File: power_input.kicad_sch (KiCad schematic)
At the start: 17 parts, among them J4 12V -, J5 12V +, U6 TPS565242

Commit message: latest
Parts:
- removed D6: SS54, Diode_SMD:D_SMA, symbol Device:D_Schottky
- added C41, C42: 100nF, Capacitor_SMD:C_0402_1005Metric, symbol Device:C_Small
- added D15: LED, LED_SMD:LED_0805_2012Metric, symbol Device:LED
- added D6: MMSZ18T1G, Diode_SMD:D_SOD-123, symbol Device:D_Zener
- added Q1: AONR21321, Transistor_Power_Module:TRANS_AONR21321, symbol AONR21321:AONR21321
- added R7: 470, Resistor_SMD:R_0603_1608Metric, symbol Device:R_Small_US
- added R9: 100K, Resistor_SMD:R_0402_1005Metric, symbol Device:R_Small_US
- C25, C26: value 10µF -> 10uF
- C27: value 0.1µF -> 100nF
- C28, C29, C30: value 22µF -> 22uF
- FB1: value 600R/3A -> HCB3216KF-601T30; footprint Capacitor_SMD:C_0805_2012Metric -> Capacitor_SMD:C_1206_3216Metric
- R11: value 20KΩ -> 20K
- R12, R14: value 30KΩ -> 30K; footprint Resistor_SMD:R_0402_1005Metric -> Resistor_SMD:R_0603_1608Metric
- R13: value 220KΩ -> 220K; footprint Resistor_SMD:R_0402_1005Metric -> Resistor_SMD:R_0603_1608Metric
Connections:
- net +5V: now also R7.2
- net WG_+12V: now also C42.1, D6.1 (K), Q1.1, Q1.2, Q1.3
- net at J5.1 (Pin_1): now also C41.1, Q1.5, Q1.6, Q1.7, Q1.8, Q1.9, Q1.9_1, Q1.9_2
- new net: D6.2 (A), Q1.4, R9.2
- new net: D15.2 (A), R7.1
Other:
- moved on the sheet: J4, J5

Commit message: starting pd chip
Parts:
- added C45, C46: 1uF, symbol Device:C_Small
- added U11: XC6206PxxxMR, Package_TO_SOT_SMD:SOT-23-3, symbol Regulator_Linear:XC6206PxxxMR
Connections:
- net +5V: now also C45.1, U11.3 (VI)
- new net +3V3: C46.1, U11.2 (VO)

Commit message: added footprints, minor deletions
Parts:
- C45, C46: footprint (none) -> Capacitor_SMD:C_0402_1005Metric
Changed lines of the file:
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@@
 			)
 		)
-		(property "Footprint" ""
+		(property "Footprint" "Capacitor_SMD:C_0402_1005Metric"
 			(at 168.91 66.04 0)
 			(effects
@@
 			)
 		)
-		(property "Footprint" ""
+		(property "Footprint" "Capacitor_SMD:C_0402_1005Metric"
 			(at 146.05 66.04 0)
 			(effects

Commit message: add usb-c-pd routing
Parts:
- D15: footprint LED_SMD:LED_0805_2012Metric -> LED_SMD:LED_0603_1608Metric
- R7: footprint Resistor_SMD:R_0603_1608Metric -> Resistor_SMD:R_0402_1005Metric
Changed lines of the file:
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@@
 			)
 		)
-		(property "Footprint" "Resistor_SMD:R_0603_1608Metric"
+		(property "Footprint" "Resistor_SMD:R_0402_1005Metric"
 			(at 100.33 74.93 0)
 			(effects
@@
 			)
 		)
-		(property "Footprint" "LED_SMD:LED_0805_2012Metric"
+		(property "Footprint" "LED_SMD:LED_0603_1608Metric"
 			(at 93.98 74.93 0)
 			(effects

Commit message: new buck
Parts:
- removed D5: 1N4148WS, Diode_SMD:D_SOD-323, symbol Diode:1N4148WS
- removed R14: 30K, Resistor_SMD:R_0603_1608Metric, symbol Device:R_Small_US
- removed U6: TPS565242, Package_TO_SOT_SMD:SOT6_DRL_TEX-L, symbol Regulator_Switching:TPS565242
- added C59, C60: 22 uF, symbol Device:C_Small
- added U6: LMR33640ADDA, Package_SO:Texas_HSOP-8-1EP_3.9x4.9mm_P1.27mm_ThermalVias, symbol Regulator_Switching:LMR33640ADDA
- C25: value 10uF -> 220 nF
- C26: value 10uF -> 10 uF
- C27: value 100nF -> 1 uF
- C28: value 22uF -> 100 nF; footprint Capacitor_SMD:C_0603_1608Metric -> (none)
- C29, C30: value 22uF -> 22 uF; footprint Capacitor_SMD:C_0603_1608Metric -> (none)
- L1: value SPM6530T-2R2M -> L; footprint Inductor_SMD:IND_SPM6530T-2R2M -> (none)
- R11: value 20K -> 100k
- R12: value 30K -> 100k; footprint Resistor_SMD:R_0603_1608Metric -> (none)
- R13: value 220K -> 24.9k; footprint Resistor_SMD:R_0603_1608Metric -> (none)
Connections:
- net WG_+12V: now also U6.2 (VIN), U6.3 (EN); no longer C27.1, R11.1
- net at C29.1, C30.1, FB1.2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: now also R12.1, C59.1, C60.1; no longer C28.1, R13.2
- net at L1.1: now also C28.2, U6.8 (SW)
- net at R11.2: now also C27.1, U6.6 (VCC); no longer R12.1
- net at R13.1: now also R12.2, U6.5 (FB)
- net at C26.2: now also C25.2
- new net: U6.1 (GND), U6.9 (GND)
- new net: R11.1, U6.4 (PG)
- new net: C28.1, U6.7 (BOOT)
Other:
- moved on the sheet: FB1

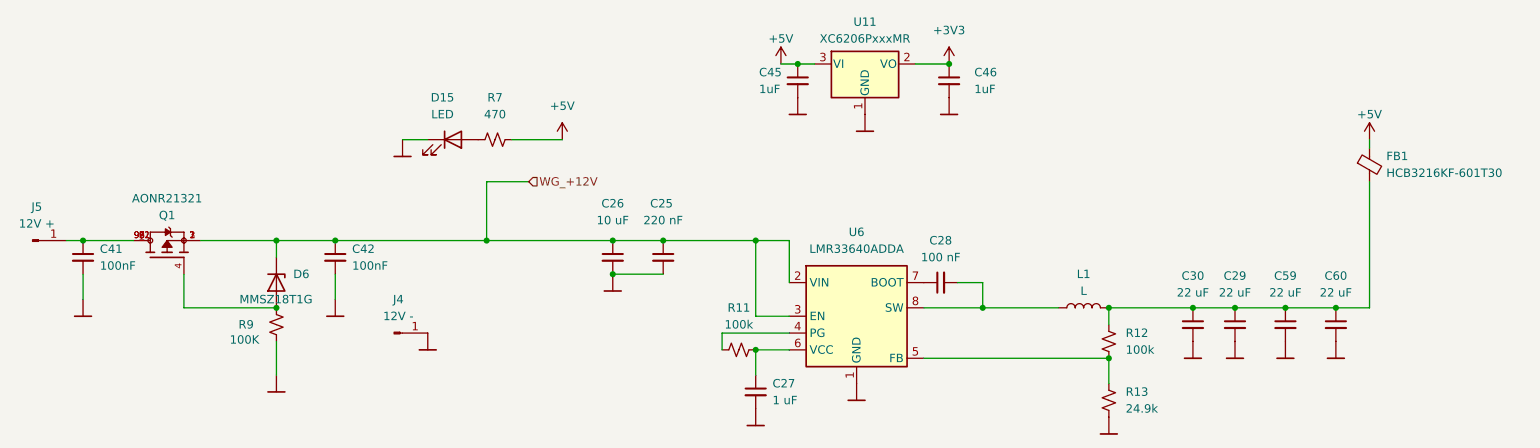
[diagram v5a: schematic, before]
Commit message: new power supply
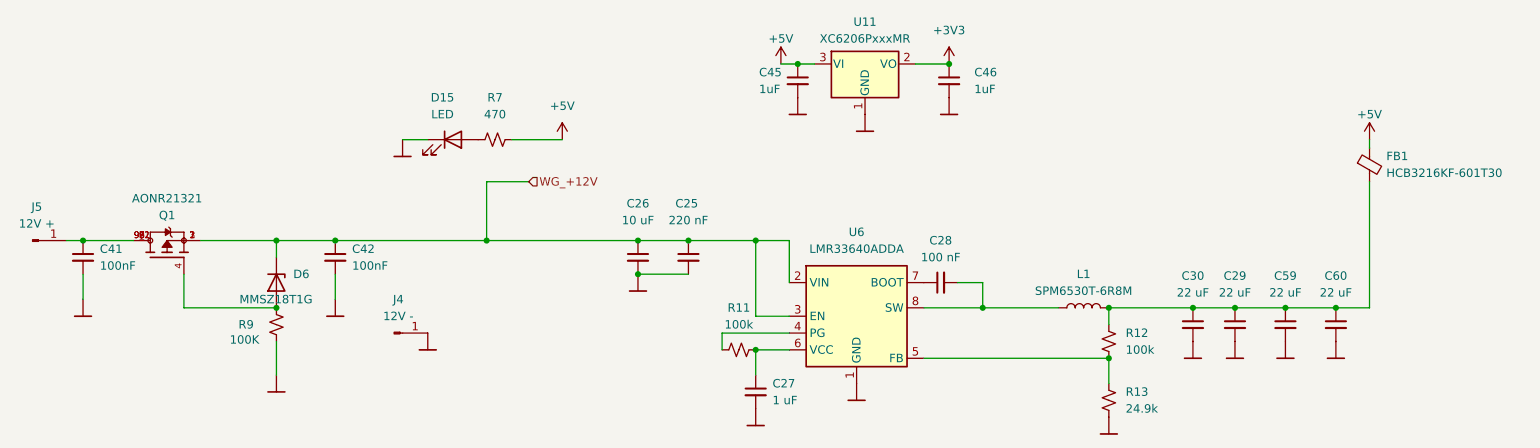
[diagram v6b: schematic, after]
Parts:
- C28, C29, C30, C59, C60, R12: footprint (none) -> Capacitor_SMD:C_0402_1005Metric
- L1: value L -> SPM6530T-6R8M; footprint (none) -> Inductor_SMD:IND_SPM6530T-2R2M
- R13: footprint (none) -> Resistor_SMD:R_0402_1005Metric
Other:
- moved on the sheet: C25, C26
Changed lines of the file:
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@@
 	)
 	(junction
+		(at 121.92 95.25)
+		(diameter 0)
+		(color 0 0 0 0)
+	)
+	(junction
+		(at 129.54 90.17)
+		(diameter 0)
+		(color 0 0 0 0)
+	)
+	(junction
 		(at 76.2 90.17)
 		(diameter 0)
@@
 	)
 	(junction
-		(at 118.11 90.17)
+		(at 99.06 90.17)
 		(diameter 0)
 		(color 0 0 0 0)
 	)
 	(junction
-		(at 99.06 90.17)
+		(at 121.92 90.17)
 		(diameter 0)
 		(color 0 0 0 0)
@@
 	)
 	(junction
-		(at 125.73 90.17)
-		(diameter 0)
-		(color 0 0 0 0)
-	)
-	(junction
 		(at 38.1 90.17)
 		(diameter 0)
@@
 	)
 	(junction
-		(at 118.11 95.25)
-		(diameter 0)
-		(color 0 0 0 0)
-	)
-	(junction
 		(at 205.74 100.33)
 		(diameter 0)
@@
 	(wire
 		(pts
-			(xy 125.73 90.17) (xy 139.7 90.17)
-		)
-		(stroke
-			(width 0)
-			(type default)
-		)
-	)
-	(wire
-		(pts
 			(xy 67.31 90.17) (xy 67.31 92.71)
 		)
@@
 	(wire
 		(pts
-			(xy 99.06 90.17) (xy 118.11 90.17)
+			(xy 99.06 90.17) (xy 121.92 90.17)
 		)
 		(stroke
@@
 	(wire
 		(pts
-			(xy 118.11 95.25) (xy 125.73 95.25)
-		)
-		(stroke
-			(width 0)
-			(type default)
-		)
-	)
-	(wire
-		(pts
 			(xy 134.62 104.14) (xy 134.62 106.68)
 		)
@@
 	(wire
 		(pts
-			(xy 118.11 90.17) (xy 125.73 90.17)
+			(xy 121.92 90.17) (xy 129.54 90.17)
 		)
 		(stroke
@@
 	(wire
 		(pts
+			(xy 129.54 90.17) (xy 139.7 90.17)
+		)
+		(stroke
+			(width 0)
+			(type default)
+		)
+	)
+	(wire
+		(pts
+			(xy 121.92 95.25) (xy 129.54 95.25)
+		)
+		(stroke
+			(width 0)
+			(type default)
+		)
+	)
+	(wire
+		(pts
 			(xy 67.31 90.17) (xy 76.2 90.17)
 		)
@@
 		(dnp no)
 		(fields_autoplaced yes)
-		(property "Reference" "01"
+		(property "Reference" "#0120"
 			(at 193.04 119.38 0)
 			(effects
@@
 			(project ""
 				(path "/6ff0ef20-ee81-4b16-8d31-a8f0cc267b22/8f744145-cbac-43cd-8d9b-32558df82040"
-					(reference "01")
+					(reference "#0120")
 					(unit 1)
 				)
@@
 		(dnp no)
 		(fields_autoplaced yes)
-		(property "Reference" "01"
+		(property "Reference" "#0112"
 			(at 154.94 114.3 0)
 			(effects
@@
 			(project ""
 				(path "/6ff0ef20-ee81-4b16-8d31-a8f0cc267b22/8f744145-cbac-43cd-8d9b-32558df82040"
-					(reference "01")
+					(reference "#0112")
 					(unit 1)
 				)
@@
 			)
 		)
-		(property "Footprint" ""
+		(property "Footprint" "Resistor_SMD:R_0402_1005Metric"
 			(at 193.04 114.3 0)
 			(effects
@@
 			)
 		)
-		(property "Footprint" ""
+		(property "Footprint" "Capacitor_SMD:C_0402_1005Metric"
 			(at 193.04 105.41 0)
 			(effects
@@
 		(dnp no)
 		(fields_autoplaced yes)
-		(property "Reference" "0101"
+		(property "Reference" "#0122"
 			(at 212.09 107.95 0)
 			(effects
@@
 			(project "wind board"
 				(path "/6ff0ef20-ee81-4b16-8d31-a8f0cc267b22/8f744145-cbac-43cd-8d9b-32558df82040"
-					(reference "0101")
+					(reference "#0122")
 					(unit 1)
 				)
@@
 	(symbol
 		(lib_id "Device:C_Small")
-		(at 125.73 92.71 0)
+		(at 129.54 92.71 0)
 		(unit 1)
 		(exclude_from_sim no)
@@
 		(dnp no)
 		(property "Reference" "C25"
-			(at 125.476 84.582 0)
+			(at 129.286 84.582 0)
 			(effects
 				(font
@@
 		)
 		(property "Value" "220 nF"
-			(at 125.73 87.122 0)
+			(at 129.54 87.122 0)
 			(effects
 				(font
@@
 		)
 		(property "Footprint" "Capacitor_SMD:C_0402_1005Metric"
-			(at 125.73 92.71 0)
+			(at 129.54 92.71 0)
 			(effects
 				(font
@@
 		)
 		(property "Datasheet" "~"
-			(at 125.73 92.71 0)
+			(at 129.54 92.71 0)
 			(effects
 				(font
@@
 		)
 		(property "Description" "Unpolarized capacitor, small symbol"
-			(at 125.73 92.71 0)
+			(at 129.54 92.71 0)
 			(effects
 				(font
@@
 			)
 		)
-		(property "Footprint" ""
+		(property "Footprint" "Capacitor_SMD:C_0402_1005Metric"
 			(at 227.33 102.87 0)
 			(effects
@@
 		(dnp no)
 		(fields_autoplaced yes)
-		(property "Reference" "0101"
+		(property "Reference" "#0123"
 			(at 205.74 107.95 0)
 			(effects
@@
 			(project "wind board"
 				(path "/6ff0ef20-ee81-4b16-8d31-a8f0cc267b22/8f744145-cbac-43cd-8d9b-32558df82040"
-					(reference "0101")
+					(reference "#0123")
 					(unit 1)
 				)
@@
 		(dnp no)
 		(fields_autoplaced yes)
-		(property "Reference" "01"
+		(property "Reference" "#0113"
 			(at 139.7 118.11 0)
 			(effects
@@
 			(project ""
 				(path "/6ff0ef20-ee81-4b16-8d31-a8f0cc267b22/8f744145-cbac-43cd-8d9b-32558df82040"
-					(reference "01")
+					(reference "#0113")
 					(unit 1)
 				)
@@
 			)
 		)
-		(property "Footprint" ""
+		(property "Footprint" "Capacitor_SMD:C_0402_1005Metric"
 			(at 205.74 102.87 0)
 			(effects
@@
 		(dnp no)
 		(fields_autoplaced yes)
-		(property "Reference" "0101"
+		(property "Reference" "#0126"
 			(at 219.71 107.95 0)
 			(effects
@@
 			(project "wind board"
 				(path "/6ff0ef20-ee81-4b16-8d31-a8f0cc267b22/8f744145-cbac-43cd-8d9b-32558df82040"
-					(reference "0101")
+					(reference "#0126")
 					(unit 1)
 				)
@@
 		(dnp no)
 		(fields_autoplaced yes)
-		(property "Reference" "01"
+		(property "Reference" "#0121"
 			(at 227.33 107.95 0)
 			(effects
@@
 			(project ""
 				(path "/6ff0ef20-ee81-4b16-8d31-a8f0cc267b22/8f744145-cbac-43cd-8d9b-32558df82040"
-					(reference "01")
+					(reference "#0121")
 					(unit 1)
 				)
@@
 			)
 		)
-		(property "Footprint" ""
+		(property "Footprint" "Capacitor_SMD:C_0402_1005Metric"
 			(at 219.71 102.87 0)
 			(effects
@@
 	(symbol
 		(lib_id "Device:C_Small")
-		(at 118.11 92.71 0)
+		(at 121.92 92.71 0)
 		(unit 1)
 		(exclude_from_sim no)
@@
 		(dnp no)
 		(property "Reference" "C26"
-			(at 118.11 84.582 0)
+			(at 121.92 84.582 0)
 			(effects
 				(font
@@
 		)
 		(property "Value" "10 uF"
-			(at 118.11 87.122 0)
+			(at 121.92 87.122 0)
 			(effects
 				(font
@@
 		)
 		(property "Footprint" "Capacitor_SMD:C_0402_1005Metric"
-			(at 118.11 92.71 0)
+			(at 121.92 92.71 0)
 			(effects
 				(font
@@
 		)
 		(property "Datasheet" "~"
-			(at 118.11 92.71 0)
+			(at 121.92 92.71 0)
 			(effects
 				(font
@@
 		)
 		(property "Description" "Unpolarized capacitor, small symbol"
-			(at 118.11 92.71 0)
+			(at 121.92 92.71 0)
 			(effects
 				(font
@@
 	(symbol
 		(lib_id "power:GND")
-		(at 118.11 97.79 0)
+		(at 121.92 97.79 0)
 		(unit 1)
 		(exclude_from_sim no)
@@
 		(dnp no)
 		(fields_autoplaced yes)
-		(property "Reference" "01"
-			(at 118.11 97.79 0)
+		(property "Reference" "#0124"
+			(at 121.92 97.79 0)
 			(effects
 				(font
@@
 		)
 		(property "Value" "~"
-			(at 118.11 100.33 0)
+			(at 121.92 100.33 0)
 			(effects
 				(font
@@
 		)
 		(property "Footprint" ""
-			(at 118.11 97.79 0)
+			(at 121.92 97.79 0)
 			(effects
 				(font
@@
 		)
 		(property "Datasheet" ""
-			(at 118.11 97.79 0)
+			(at 121.92 97.79 0)
 			(effects
 				(font
@@
 		)
 		(property "Description" "GND"
-			(at 118.11 97.79 0)
+			(at 121.92 97.79 0)
 			(effects
 				(font
@@
 			(project ""
 				(path "/6ff0ef20-ee81-4b16-8d31-a8f0cc267b22/8f744145-cbac-43cd-8d9b-32558df82040"
-					(reference "01")
+					(reference "#0124")
 					(unit 1)
 				)
@@
 			)
 		)
-		(property "Value" "L"
+		(property "Value" "SPM6530T-6R8M"
 			(at 189.23 97.79 90)
 			(effects
@@
 			)
 		)
-		(property "Footprint" ""
+		(property "Footprint" "Inductor_SMD:IND_SPM6530T-2R2M"
 			(at 189.23 100.33 0)
 			(effects
@@
 			)
 		)
-		(property "Footprint" ""
+		(property "Footprint" "Capacitor_SMD:C_0402_1005Metric"
 			(at 212.09 102.87 0)
 			(effects
@@
 			)
 		)
-		(property "Footprint" ""
+		(property "Footprint" "Capacitor_SMD:C_0402_1005Metric"
 			(at 167.64 96.52 0)
 			(effects

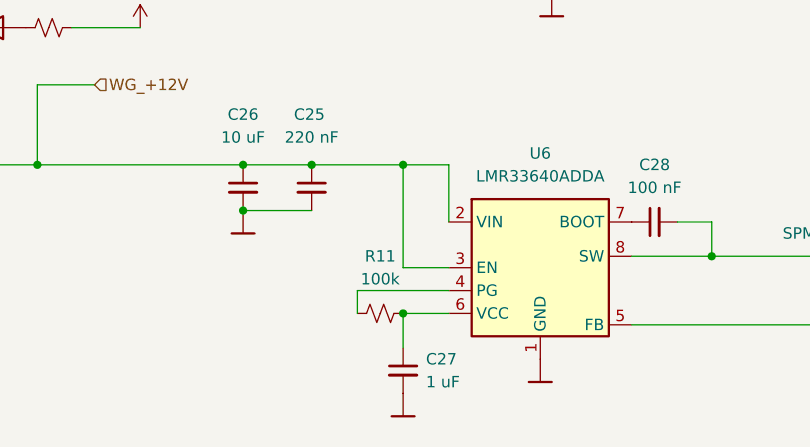
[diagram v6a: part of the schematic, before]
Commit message: remove pullup resistor
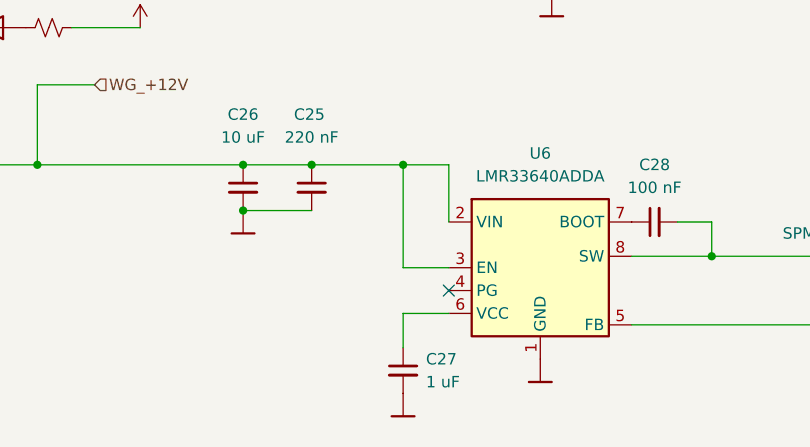
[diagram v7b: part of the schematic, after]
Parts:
- removed R11: 100k, Resistor_SMD:R_0402_1005Metric, symbol Device:R_Small_US
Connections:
- no-connect marks 0 -> 1
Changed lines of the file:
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@@
 	)
 	(junction
-		(at 139.7 106.68)
-		(diameter 0)
-		(color 0 0 0 0)
-	)
-	(junction
 		(at 67.31 100.33)
 		(diameter 0)
@@
 		(color 0 0 0 0)
 	)
+	(no_connect
+		(at 144.78 104.14)
+	)
 	(wire
 		(pts
@@
 	(wire
 		(pts
-			(xy 134.62 104.14) (xy 134.62 106.68)
-		)
-		(stroke
-			(width 0)
-			(type default)
-		)
-	)
-	(wire
-		(pts
 			(xy 99.06 81.28) (xy 105.41 81.28)
 		)
@@
 	(wire
 		(pts
-			(xy 144.78 104.14) (xy 134.62 104.14)
-		)
-		(stroke
-			(width 0)
-			(type default)
-		)
-	)
-	(wire
-		(pts
 			(xy 143.51 63.5) (xy 146.05 63.5)
 		)
@@
 					(unit 1)
 				)
-			)
-		)
-	)
-	(symbol
-		(lib_id "Device:R_Small_US")
-		(at 137.16 106.68 90)
-		(unit 1)
-		(exclude_from_sim no)
-		(in_bom yes)
-		(on_board yes)
-		(dnp no)
-		(property "Reference" "R11"
-			(at 137.16 100.33 90)
-			(effects
-				(font
-					(size 1.27 1.27)
-				)
-			)
-		)
-		(property "Value" "100k"
-			(at 137.16 102.87 90)
-			(effects
-				(font
-					(size 1.27 1.27)
-				)
-			)
-		)
-		(property "Footprint" "Resistor_SMD:R_0402_1005Metric"
-			(at 137.16 106.68 0)
-			(effects
-				(font
-					(size 1.27 1.27)
-				)
-				(hide yes)
-			)
-		)
-		(property "Datasheet" "~"
-			(at 137.16 106.68 0)
-			(effects
-				(font
-					(size 1.27 1.27)
-				)
-				(hide yes)
-			)
-		)
-		(property "Description" "Resistor, small US symbol"
-			(at 137.16 106.68 0)
-			(effects
-				(font
-					(size 1.27 1.27)
-				)
-				(hide yes)
-			)
-		)
-		(pin "1"
-		)
-		(pin "2"
-		)
-		(instances
-			(project ""
-				(path "/6ff0ef20-ee81-4b16-8d31-a8f0cc267b22/8f744145-cbac-43cd-8d9b-32558df82040"
-					(reference "R11")
-					(unit 1)
-				)
